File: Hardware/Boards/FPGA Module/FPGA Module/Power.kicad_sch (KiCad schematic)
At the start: 157 parts, among them U10 L78L33_SOT89, U11 INA236, U13 INA700AYWFR, U15 INA700AYWFR, U17 INA700AYWFR, U19 INA700AYWFR, U24 MP8796, U25 MP8796, U9 LT7200S

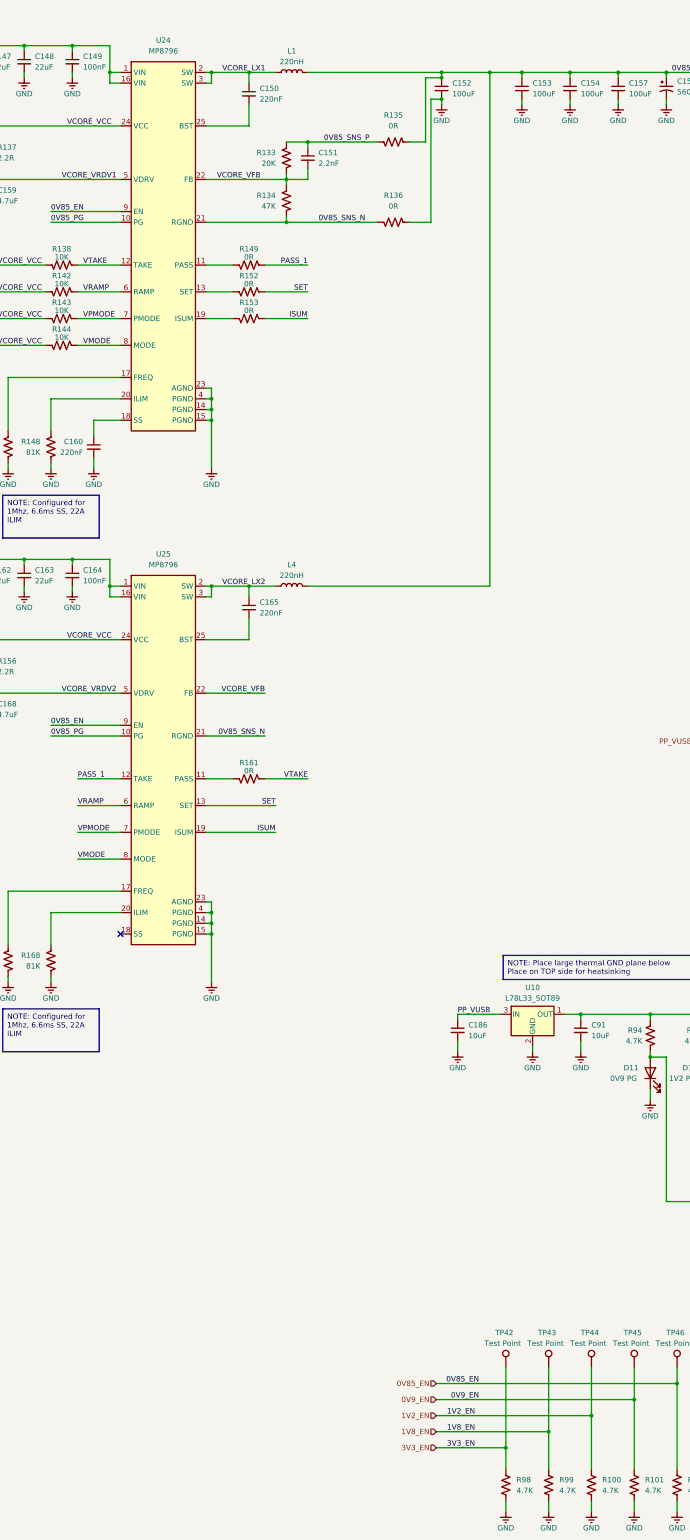
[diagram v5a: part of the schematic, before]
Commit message: Updated SCH and Layout
Added temp sensors for DCDC's, Added MCU control for FPGA mode, removed mode DIP switch
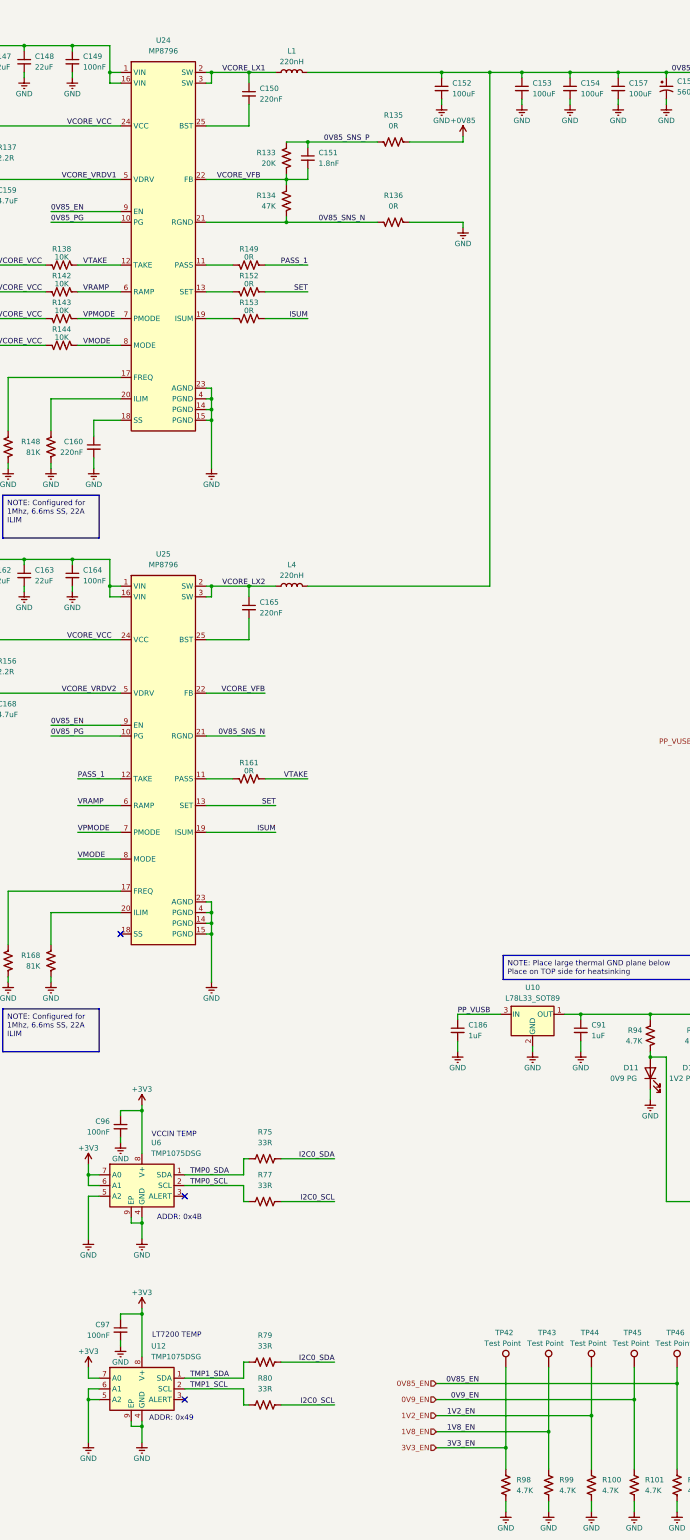
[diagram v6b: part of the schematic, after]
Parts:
- added C96, C97: 100nF, Capacitor_SMD:C_0201_0603Metric, symbol Device:C_Small
- added R75, R77, R79, R80: 33R, Resistor_SMD:R_0201_0603Metric, symbol Device:R_US
- added U12, U6: TMP1075DSG, Package_SON:WSON-8-1EP_2x2mm_P0.5mm_EP0.9x1.6mm_ThermalVias, symbol Sensor_Temperature:TMP1075DSG
- C151: value 2.2nF -> 1.8nF
- C186, C91: value 10uF -> 1uF
- C87, C92: footprint Capacitor_SMD:C_0402_1005Metric -> Capacitor_SMD:C_0201_0603Metric
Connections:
- net +0V85: now also R135.1
- net +3V3: now also C96.1, C97.1, U12.7 (A0), U12.8 (V+), U6.6 (A1), U6.7 (A0), U6.8 (V+)
- net 0V85_SNS: no longer R135.1
- net GND: now also C96.2, C97.2, U12.4 (GND), U12.5 (A2), U12.6 (A1), U12.9 (EP), U6.4 (GND), U6.5 (A2), U6.9 (EP)
- net I2C0_SCL: now also R77.2, R80.2
- net I2C0_SDA: now also R75.2, R79.2
- new net TMP0_SCL: R77.1, U6.2 (SCL)
- new net TMP0_SDA: R75.1, U6.1 (SDA)
- new net TMP1_SCL: R80.1, U12.2 (SCL)
- new net TMP1_SDA: R79.1, U12.1 (SDA)
- no-connect marks 1 -> 3
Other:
- note added: "ADDR: 0x49"
- note added: "ADDR: 0x4B"
- note added: "LT7200 TEMP"
- note added: "VCCIN TEMP"

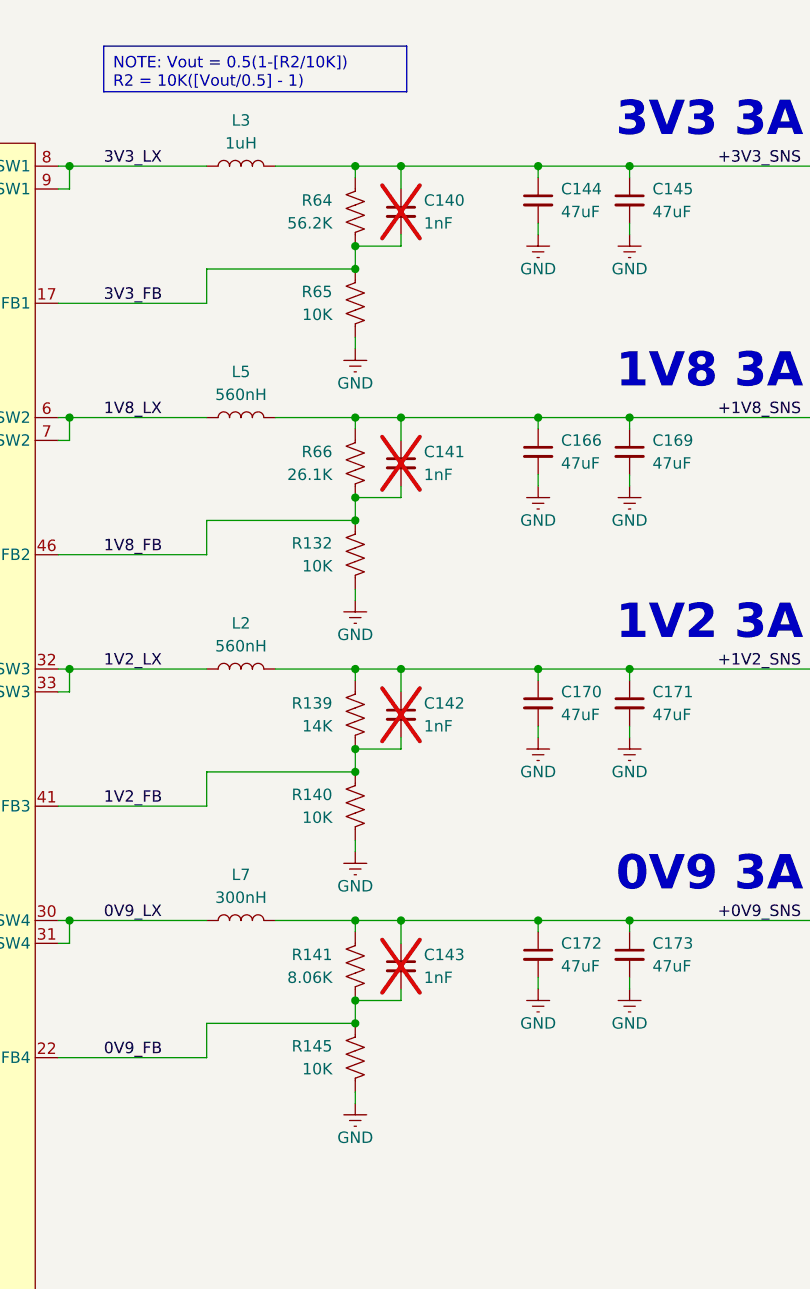
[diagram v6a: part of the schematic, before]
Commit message: Updated FPGA Module Routing
Cleaned up routing
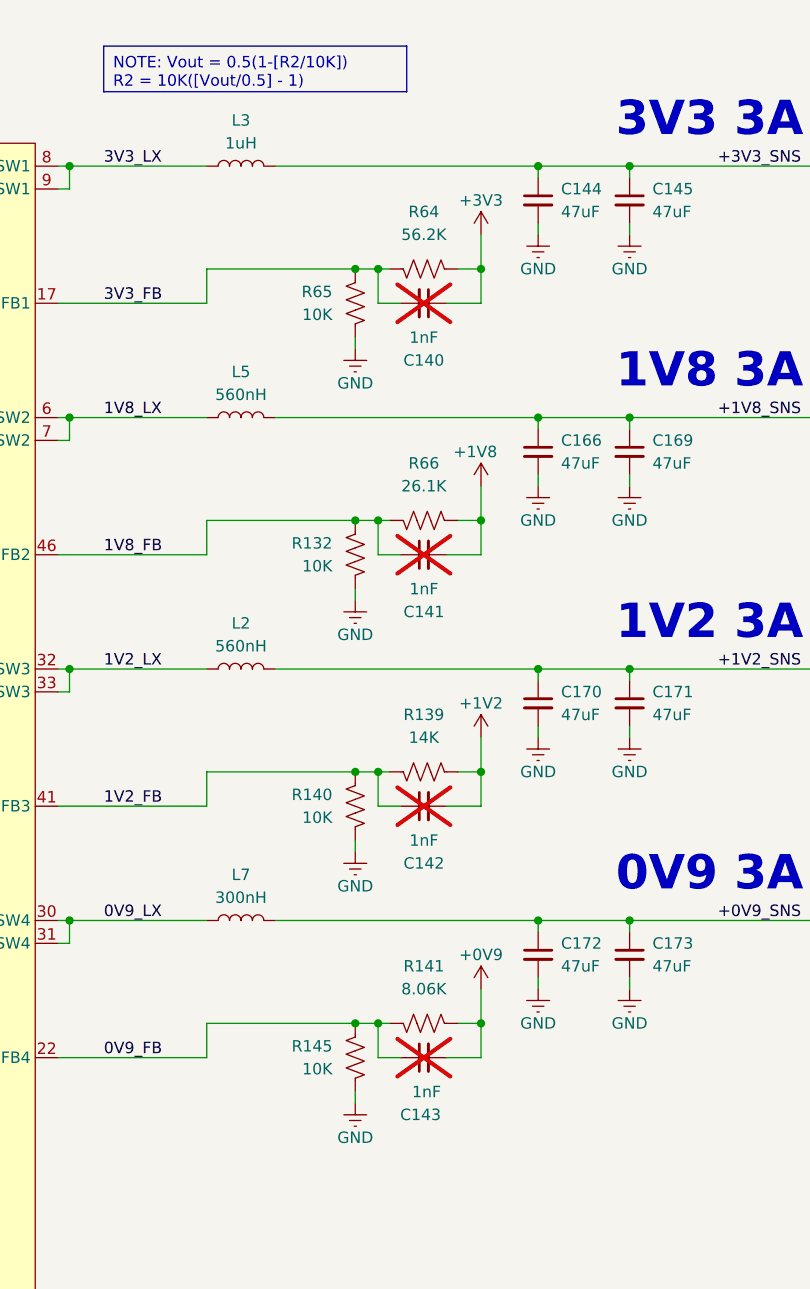
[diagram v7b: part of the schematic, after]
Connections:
- net +0V9: now also C143.2, R141.1
- net +0V9_SNS: no longer C143.1, R141.2
- net +1V2: now also C142.2, R139.1
- net +1V2_SNS: no longer C142.1, R139.2
- net +1V8: now also C141.2, R66.1
- net +1V8_SNS: no longer C141.1, R66.2
- net +3V3: now also C140.1, R64.1
- net +3V3_SNS: no longer C140.1, R64.2
- net 0V9_FB: now also C143.1, R141.2; no longer C143.2, R141.1
- net 1V2_FB: now also C142.1, R139.2; no longer C142.2, R139.1
- net 1V8_FB: now also C141.1, R66.2; no longer C141.2, R66.1
- net 3V3_FB: now also R64.2; no longer R64.1
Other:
- moved on the sheet: C140, C141, C142, C143, R139, R141, R64, R66

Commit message: Updated DDR4 routing
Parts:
- C151: footprint Capacitor_SMD:C_0402_1005Metric -> Capacitor_SMD:C_0201_0603Metric
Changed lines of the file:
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@@
 			)
 		)
-		(property "Footprint" "Capacitor_SMD:C_0402_1005Metric"
+		(property "Footprint" "Capacitor_SMD:C_0201_0603Metric"
 			(at 135.89 64.77 0)
 			(effects
